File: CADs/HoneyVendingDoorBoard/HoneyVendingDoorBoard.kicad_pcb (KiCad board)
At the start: 2 copper layers, 34 parts, among them J1 Conn_01x08_Female, J2 Door5, J3 Door6, J4 Door1, J5 Door2, J6 Door3, J7 Door4, Q1 IRLZ34N, Q2 IRLZ34N, Q3 IRLZ34N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

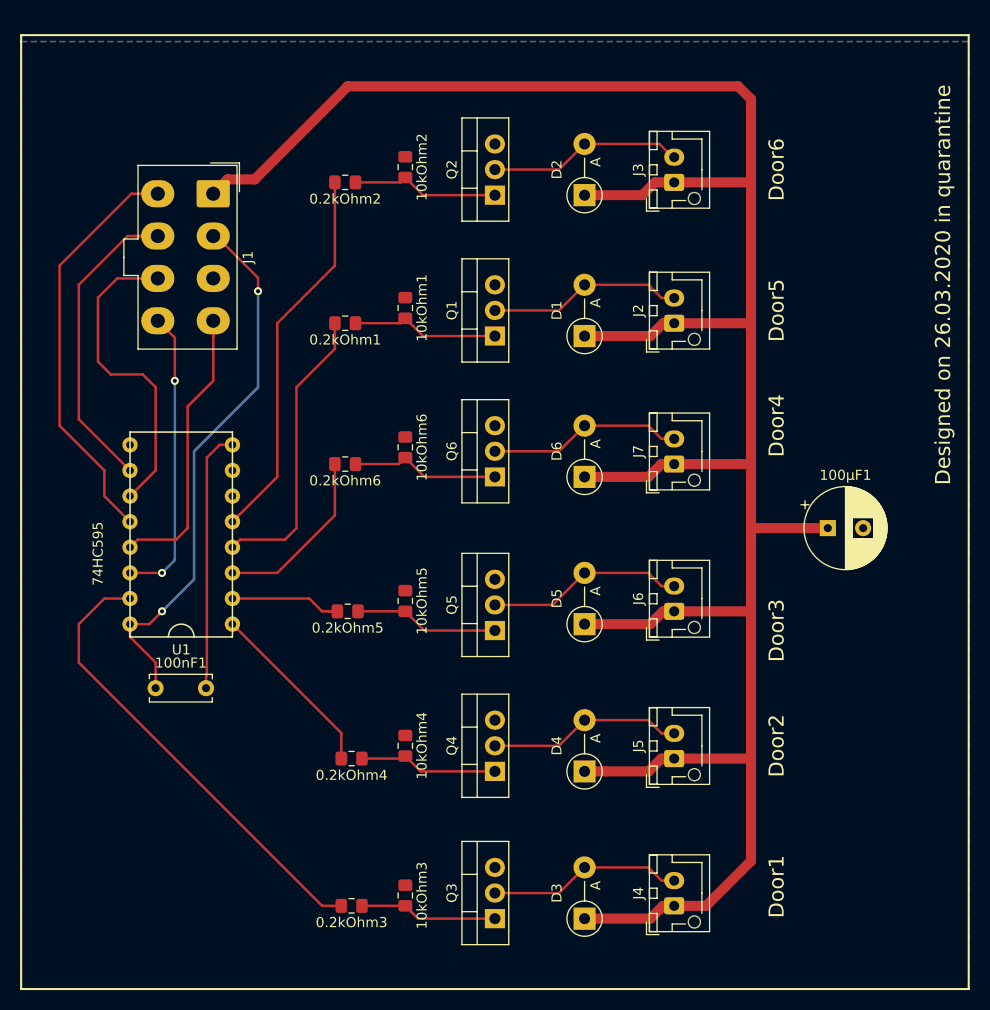
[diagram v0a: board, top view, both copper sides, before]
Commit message: Reworded PCBs and added PCB pdfs
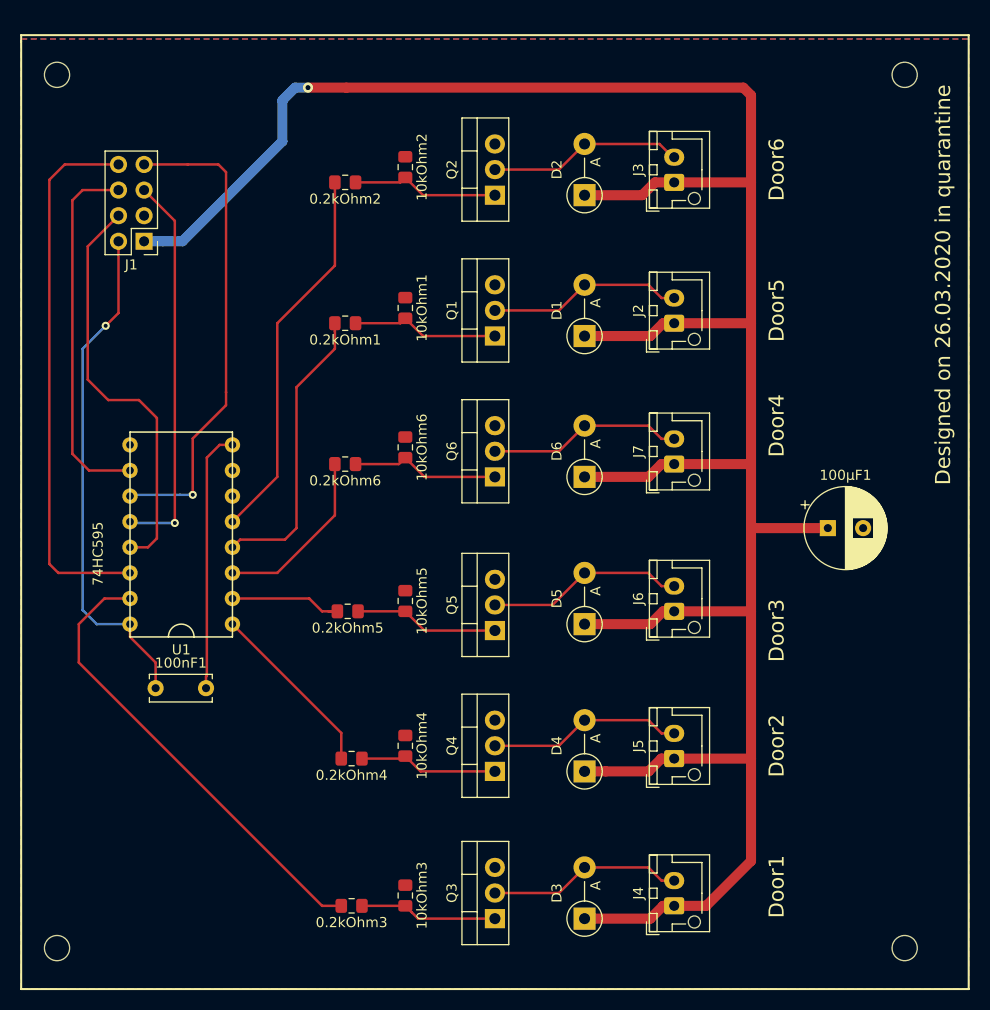
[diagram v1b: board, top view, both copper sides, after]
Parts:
- added ?: MountingHole_2.5mm, MountingHole:MountingHole_2.5mm, F.Cu at (67.1, 55.4)
- added ?: MountingHole_2.5mm, MountingHole:MountingHole_2.5mm, F.Cu at (67.1, 142.0)
- added ?: MountingHole_2.5mm, MountingHole:MountingHole_2.5mm, F.Cu at (151.1, 142.0)
- added ?: MountingHole_2.5mm, MountingHole:MountingHole_2.5mm, F.Cu at (151.1, 55.4)
- J1: footprint Connector_Molex:Molex_Mini-Fit_Jr_5566-08A_2x04_P4.20mm_Vertical -> Connector_PinHeader_2.54mm:PinHeader_2x04_P2.54mm_Vertical
- moved J1 8.32 mm to (75.7, 71.9), turned to 180 degrees
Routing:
- net Net-(J1-Pad8): track 29.4 -> 54.0 mm, vias 2 -> 0
- net Net-(J1-Pad7): track 31.7 -> 48.1 mm, vias 0 -> 1
- net +12V: track 245.5 -> 256.8 mm, vias 0 -> 1
- net Net-(J1-Pad4): track 29.7 -> 40.9 mm
- net Net-(J1-Pad6): track 32.7 -> 36.5 mm
- net +5V: track 54.3 -> 50.7 mm, vias 2 -> 1
- net Net-(J1-Pad5): track 41.0 -> 38.8 mm, vias 0 -> 1

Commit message: Updates boards
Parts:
- added 100µF1: C, Capacitor_THT:CP_Radial_D8.0mm_P3.50mm, F.Cu at (144.3, 95.5)
- J1: moved to B.Cu
- J2, J3, J4, J5, J6, J7: footprint Connector_JST:JST_XH_B02B-XH-AM_1x02_P2.50mm_Vertical -> Connector_PinHeader_2.54mm:PinHeader_1x02_P2.54mm_Vertical
- moved 100µF1 7.15 mm to (144.3, 107.4)
- moved J1 3.61 mm to (73.4, 74.7)
- moved J2 1.61 mm to (129.8, 80.5), turned to 180 degrees
- moved J5 1.55 mm to (129.8, 123.4), turned to 180 degrees
- moved J4 1.53 mm to (129.8, 137.9), turned to 180 degrees
- moved J6 1.53 mm to (129.8, 108.7), turned to 180 degrees
- moved J3 1.52 mm to (129.8, 66.0), turned to 180 degrees
- moved J7 1.52 mm to (129.8, 94.0), turned to 180 degrees
- moved U1 1.14 mm to (80.5, 99.7)
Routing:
- net Net-(J1-Pad7): track 48.1 -> 21.1 mm, vias 1 -> 0
- net Net-(J1-Pad8): track 54.0 -> 27.5 mm
- net GND: track 26.0 -> 0.00 mm
- net +12V: track 256.8 -> 269.7 mm, vias 1 -> 0
- net Net-(J1-Pad6): track 36.5 -> 24.2 mm, vias 0 -> 1
- net Net-(J1-Pad5): track 38.8 -> 29.7 mm, vias 1 -> 0
- net +5V: track 50.7 -> 58.9 mm
- net Net-(J1-Pad4): track 40.9 -> 37.6 mm, vias 0 -> 1
- net Net-(0.2kOhm3-Pad2): track 46.0 -> 48.4 mm
- net Net-(0.2kOhm2-Pad2): track 37.9 -> 39.6 mm
- net Net-(D1-Pad2): track 19.4 -> 21.1 mm
- net Net-(D4-Pad2): track 19.4 -> 21.0 mm
- net Net-(D3-Pad2): track 19.4 -> 20.9 mm
- net Net-(D5-Pad2): track 19.6 -> 21.2 mm
- net Net-(D2-Pad2): track 19.4 -> 20.9 mm
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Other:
- board text added: "GND"

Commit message: Applying nicos feedback for boards
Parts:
- added 100nF2: AntiFlicker, Capacitor_THT:C_Disc_D6.0mm_W2.5mm_P5.00mm, F.Cu at (68.5, 112.4)
- added J8: 12V Power, Connector_PinHeader_2.54mm:PinHeader_1x02_P2.54mm_Vertical, F.Cu at (133.3, 55.8)
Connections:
- net Net-(J1-Pad4) renamed /OE
- net Net-(J1-Pad5) renamed /RCLK
- net Net-(J1-Pad6) renamed /SRCLR
- net Net-(J1-Pad7) renamed /SRCLK
- net Net-(J1-Pad8) renamed /SER
- J1 pad 1: +12V -> Net-(J1-Pad1)
- J1 pad 2: +5V -> Net-(J1-Pad2)
- J1 pad 3: GND -> +5V
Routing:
- net +12V: track 269.7 -> 198.4 mm
- net +5V: track 58.9 -> 45.7 mm, vias 1 -> 2
- net /RCLK: track 29.7 -> 42.6 mm, vias 0 -> 1
- net Net-(0.2kOhm3-Pad2): track 48.4 -> 42.5 mm

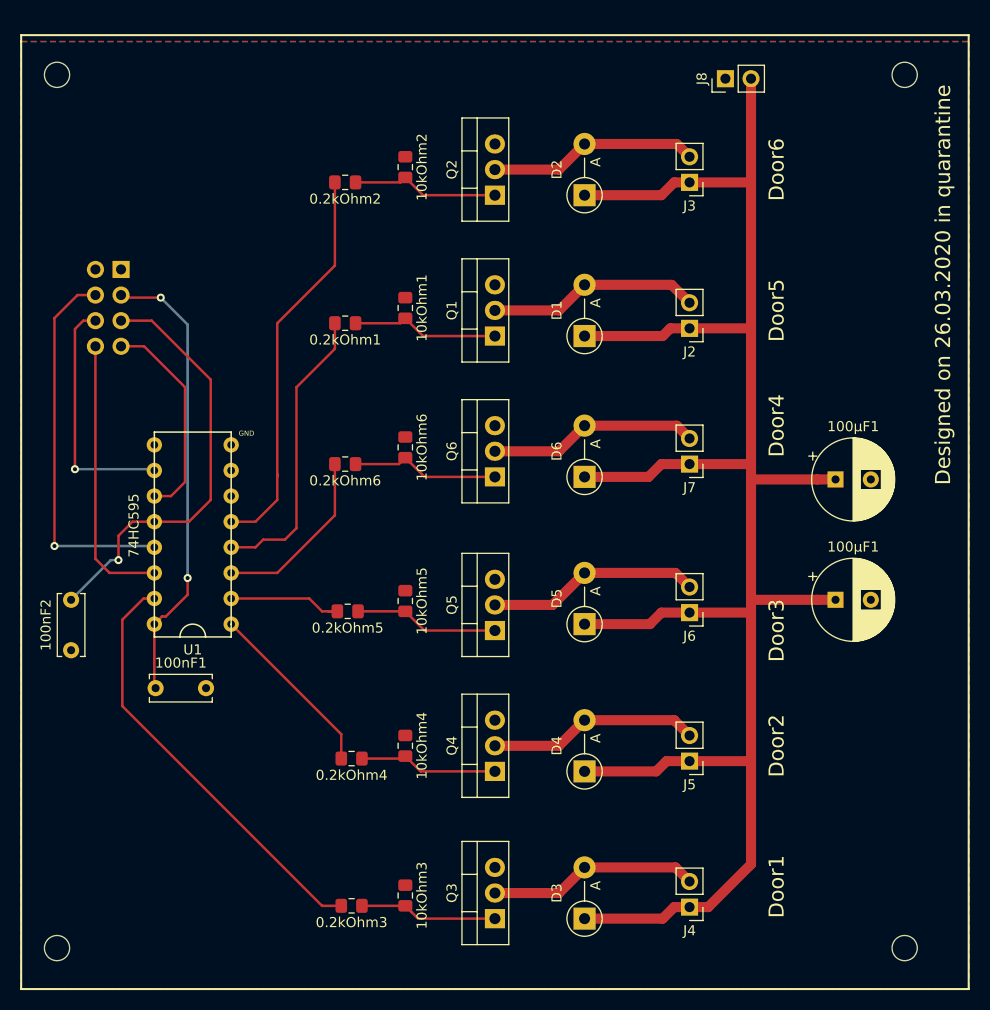
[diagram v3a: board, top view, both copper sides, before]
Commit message: Split Main Board into Main Board and Button Board
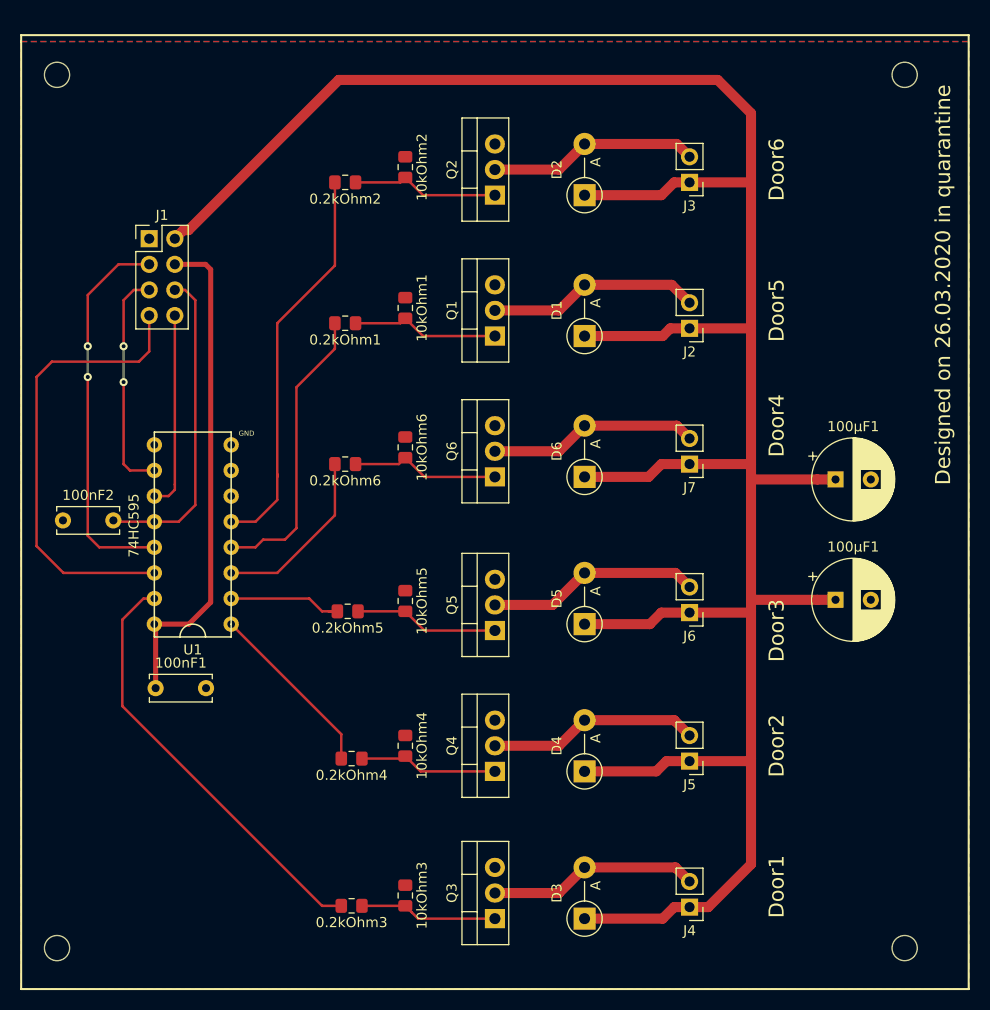
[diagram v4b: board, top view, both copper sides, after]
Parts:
- removed J8: 12V Power, Connector_PinHeader_2.54mm:PinHeader_1x02_P2.54mm_Vertical
- J1: moved to F.Cu
- moved 100nF2 12.9 mm to (67.6, 99.6), turned to 0 degrees
- moved J1 4.13 mm to (76.2, 71.6), turned to 0 degrees
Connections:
- J1 pad 1: Net-(J1-Pad1) -> GND
- J1 pad 2: Net-(J1-Pad2) -> +12V
- J1 pad 3: +5V -> /OE
- J1 pad 4: /OE -> +5V
- J1 pad 5: /RCLK -> /SRCLR
- J1 pad 6: /SRCLR -> /RCLK
- J1 pad 7: /SRCLK -> /SER
- J1 pad 8: /SER -> /SRCLK
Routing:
- net +12V: track 198.4 -> 260.0 mm
- net /SER: track 27.5 -> 45.3 mm
- net /RCLK: track 42.6 -> 31.6 mm, vias 1 -> 0
- net +5V: track 45.7 -> 50.0 mm, vias 2 -> 0
- net /SRCLR: track 24.2 -> 22.7 mm, vias 1 -> 2
- net /SRCLK: track 21.1 -> 19.6 mm
- net /OE: track 37.6 -> 38.5 mm, vias 1 -> 2
